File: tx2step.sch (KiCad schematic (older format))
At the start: 17 parts, among them IC1 ATMEGA328P-MM

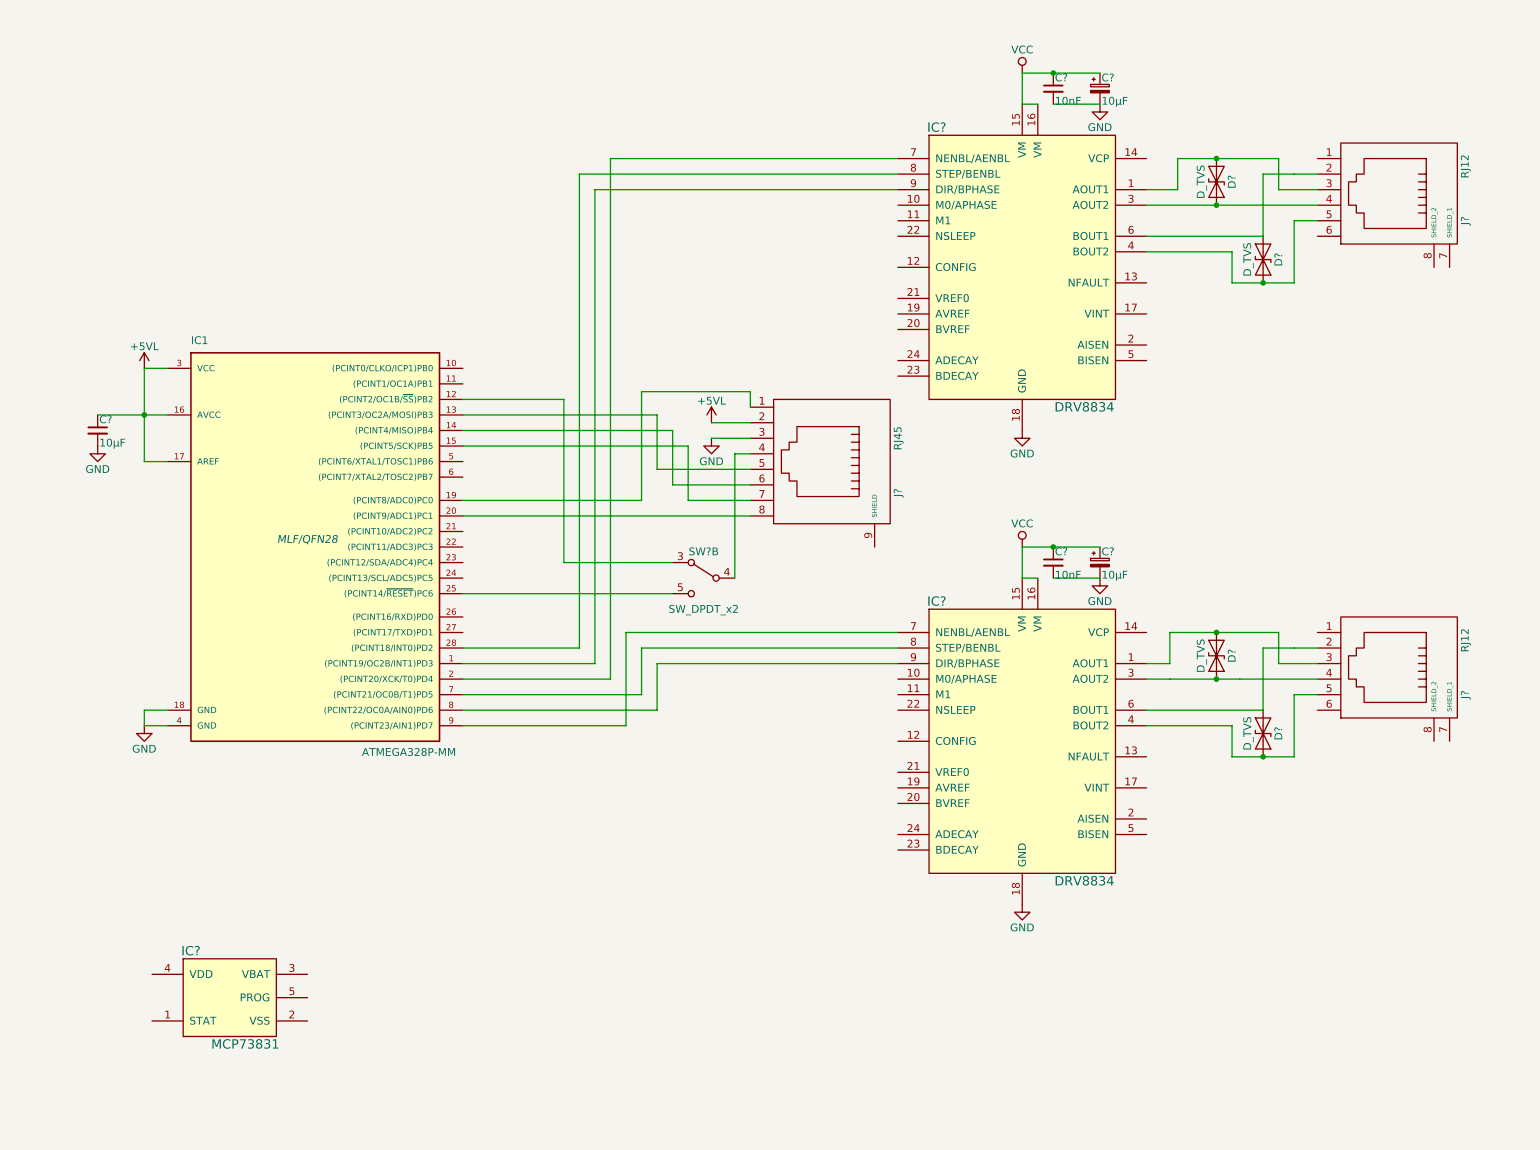
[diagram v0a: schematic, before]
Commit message: Add rate selector switches
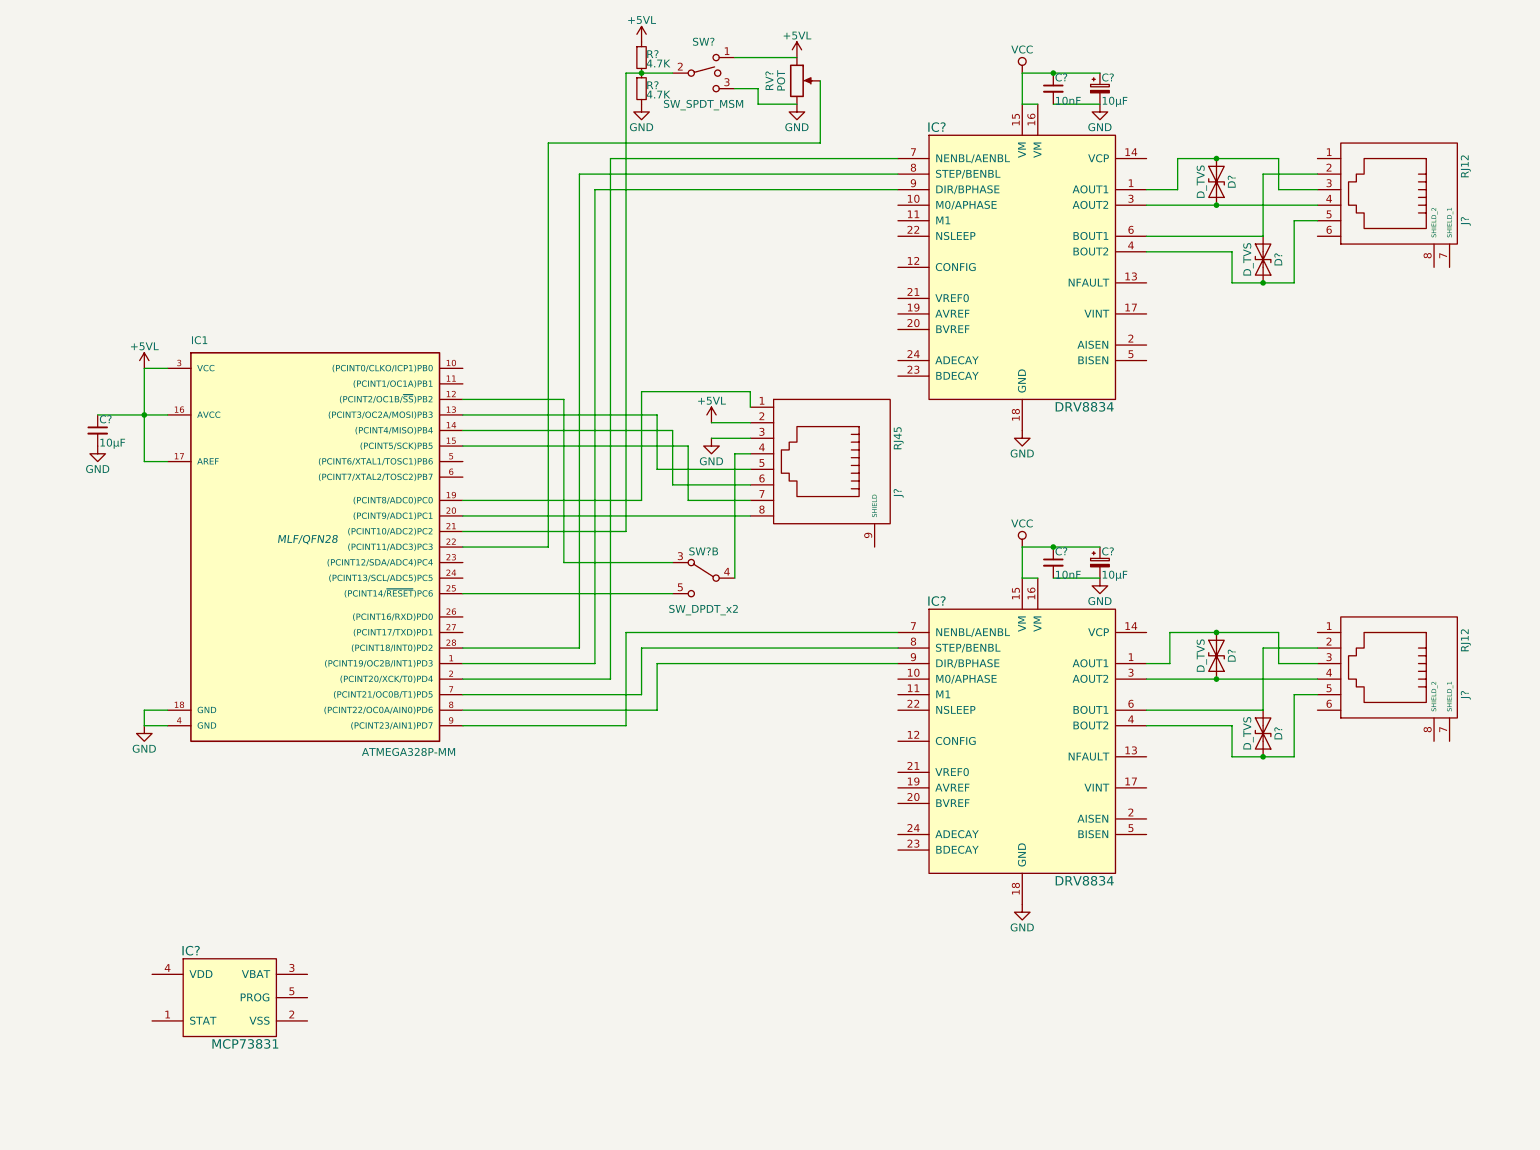
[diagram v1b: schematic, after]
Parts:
- added R? (x2): 4.7K, symbol R_Small
- added RV?: POT, symbol POT
- added SW?: SW_SPDT_MSM, symbol SW_SPDT_MSM
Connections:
- net +5VL: now also R?.1, RV?.1, SW?.1
- net GND: now also R?.2, RV?.3, SW?.3
- net at IC1.21 ((PCINT10/ADC2)PC2): now also R?.1, R?.2, SW?.2
- net at IC1.22 ((PCINT11/ADC3)PC3): now also RV?.2
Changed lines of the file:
@@
 	8150 1550 8150 1750
 Wire Wire Line
-	7950 1850 8400 1850
-Wire Wire Line
-	8400 1850 9050 1850
+	7950 1850 9050 1850
 Wire Wire Line
 	8800 1550 8800 1750
@@
 	8700 2050 8700 1650
 Wire Wire Line
-	8700 1650 8900 1650
-Wire Wire Line
-	8900 1650 8900 1650
-Wire Wire Line
-	8900 1650 9050 1650
+	8700 1650 9050 1650
 Wire Wire Line
 	9050 1950 8900 1950
 Wire Wire Line
-	8900 2350 8900 1950
-Wire Wire Line
-	8500 2350 8700 2350
-Wire Wire Line
-	8700 2350 8900 2350
+	8900 1950 8900 2350
+Wire Wire Line
+	8900 2350 8500 2350
 Wire Wire Line
 	8500 2350 8500 2150
@@
 	8100 4800 8100 4600
 Wire Wire Line
-	8100 4600 8400 4600
-Wire Wire Line
-	8400 4600 8800 4600
-Wire Wire Line
-	7950 4900 8100 4900
-Wire Wire Line
-	8100 4900 8100 4900
-Wire Wire Line
-	8100 4900 8400 4900
-Wire Wire Line
-	8400 4900 8550 4900
+	8100 4600 8800 4600
+Wire Wire Line
+	7950 4900 9050 4900
 Wire Wire Line
 	8800 4600 8800 4800
@@
 	8800 4800 9050 4800
 Connection ~ 8400 4600
-Wire Wire Line
-	8550 4900 8550 4900
-Wire Wire Line
-	8550 4900 9050 4900
 Connection ~ 8400 4900
 Wire Wire Line
@@
 	8500 5200 8500 5400
 Wire Wire Line
-	8500 5400 8700 5400
-Wire Wire Line
-	8700 5400 8900 5400
+	8500 5400 8900 5400
 Wire Wire Line
 	8700 5100 8700 4700
 Wire Wire Line
-	8700 4700 8900 4700
-Wire Wire Line
-	8900 4700 8900 4700
-Wire Wire Line
-	8900 4700 9050 4700
+	8700 4700 9050 4700
 Wire Wire Line
 	8900 5400 8900 5000
@@
 	4800 4800 6350 4800
 Wire Wire Line
-	1500 2900 1500 3200
-Wire Wire Line
-	1500 3200 1500 3500
-Wire Wire Line
-	1200 3200 1500 3200
-Wire Wire Line
-	1500 3200 1650 3200
+	1500 2900 1500 3500
+Wire Wire Line
+	1200 3200 1650 3200
 Connection ~ 1500 3200
 Wire Wire Line
@@
 	7150 4250 7250 4250
 Wire Wire Line
-	7150 1000 7350 1000
-Wire Wire Line
-	7350 1000 7650 1000
+	7150 1000 7650 1000
 Wire Wire Line
 	7150 1000 7150 1200
@@
 	7350 1200 7650 1200
 Wire Wire Line
-	7150 4050 7350 4050
-Wire Wire Line
-	7350 4050 7650 4050
+	7150 4050 7650 4050
 Wire Wire Line
 	7650 4250 7350 4250
@@
 $EndComp
 Wire Wire Line
-	8150 1550 8400 1550
-Wire Wire Line
-	8400 1550 8800 1550
+	8150 1550 8800 1550
 Connection ~ 8400 1550
 $Comp
@@
 	1    0    0    -1
 $EndComp
+$Comp
+L SW_SPDT_MSM SW?
+U 1 1 58B86814
+P 5100 1000
+F 0 "SW?" H 5100 1200 50  0000 C CNN
+F 1 "SW_SPDT_MSM" H 5100 800 50  0000 C CNN
+F 2 "" H 5100 1000 50  0001 C CNN
+F 3 "" H 5100 1000 50  0001 C CNN
+	1    5100 1000
+	1    0    0    -1
+$EndComp
+$Comp
+L POT RV?
+U 1 1 58B868AD
+P 5700 1050
+F 0 "RV?" V 5525 1050 50  0000 C CNN
+F 1 "POT" V 5600 1050 50  0000 C CNN
+F 2 "" H 5700 1050 50  0000 C CNN
+F 3 "" H 5700 1050 50  0000 C CNN
+	1    5700 1050
+	1    0    0    -1
+$EndComp
+Wire Wire Line
+	5300 900  5700 900
+Wire Wire Line
+	5300 1100 5450 1100
+Wire Wire Line
+	5450 1100 5450 1200
+Wire Wire Line
+	5450 1200 5700 1200
+$Comp
+L +5VL #PWR?
+U 1 1 58B874D3
+P 5700 900
+F 0 "#PWR?" H 5700 750 50  0001 C CNN
+F 1 "+5VL" H 5700 1040 50  0000 C CNN
+F 2 "" H 5700 900 50  0000 C CNN
+F 3 "" H 5700 900 50  0000 C CNN
+	1    5700 900
+	1    0    0    -1
+$EndComp
+$Comp
+L GND #PWR?
+U 1 1 58B87520
+P 5700 1200
+F 0 "#PWR?" H 5700 950 50  0001 C CNN
+F 1 "GND" H 5700 1050 50  0000 C CNN
+F 2 "" H 5700 1200 50  0000 C CNN
+F 3 "" H 5700 1200 50  0000 C CNN
+	1    5700 1200
+	1    0    0    -1
+$EndComp
+$Comp
+L R_Small R?
+U 1 1 58B876D6
+P 4700 900
+F 0 "R?" H 4730 920 50  0000 L CNN
+F 1 "4.7K" H 4730 860 50  0000 L CNN
+F 2 "" H 4700 900 50  0000 C CNN
+F 3 "" H 4700 900 50  0000 C CNN
+	1    4700 900
+	1    0    0    -1
+$EndComp
+$Comp
+L R_Small R?
+U 1 1 58B87737
+P 4700 1100
+F 0 "R?" H 4730 1120 50  0000 L CNN
+F 1 "4.7K" H 4730 1060 50  0000 L CNN
+F 2 "" H 4700 1100 50  0000 C CNN
+F 3 "" H 4700 1100 50  0000 C CNN
+	1    4700 1100
+	1    0    0    -1
+$EndComp
+Wire Wire Line
+	4600 1000 4900 1000
+Wire Wire Line
+	4600 3950 3550 3950
+Connection ~ 4700 1000
+Wire Wire Line
+	4100 4050 3550 4050
+Wire Wire Line
+	4100 1450 5850 1450
+Wire Wire Line
+	5850 1450 5850 1050
+$Comp
+L GND #PWR?
+U 1 1 58B895AD
+P 4700 1200
+F 0 "#PWR?" H 4700 950 50  0001 C CNN
+F 1 "GND" H 4700 1050 50  0000 C CNN
+F 2 "" H 4700 1200 50  0000 C CNN
+F 3 "" H 4700 1200 50  0000 C CNN
+	1    4700 1200
+	1    0    0    -1
+$EndComp
+$Comp
+L +5VL #PWR?
+U 1 1 58B89600
+P 4700 800
+F 0 "#PWR?" H 4700 650 50  0001 C CNN
+F 1 "+5VL" H 4700 940 50  0000 C CNN
+F 2 "" H 4700 800 50  0000 C CNN
+F 3 "" H 4700 800 50  0000 C CNN
+	1    4700 800
+	1    0    0    -1
+$EndComp
+Wire Wire Line
+	4100 1450 4100 4050
+Wire Wire Line
+	4600 1000 4600 3950
 $EndSCHEMATC

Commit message: Add clock crystal
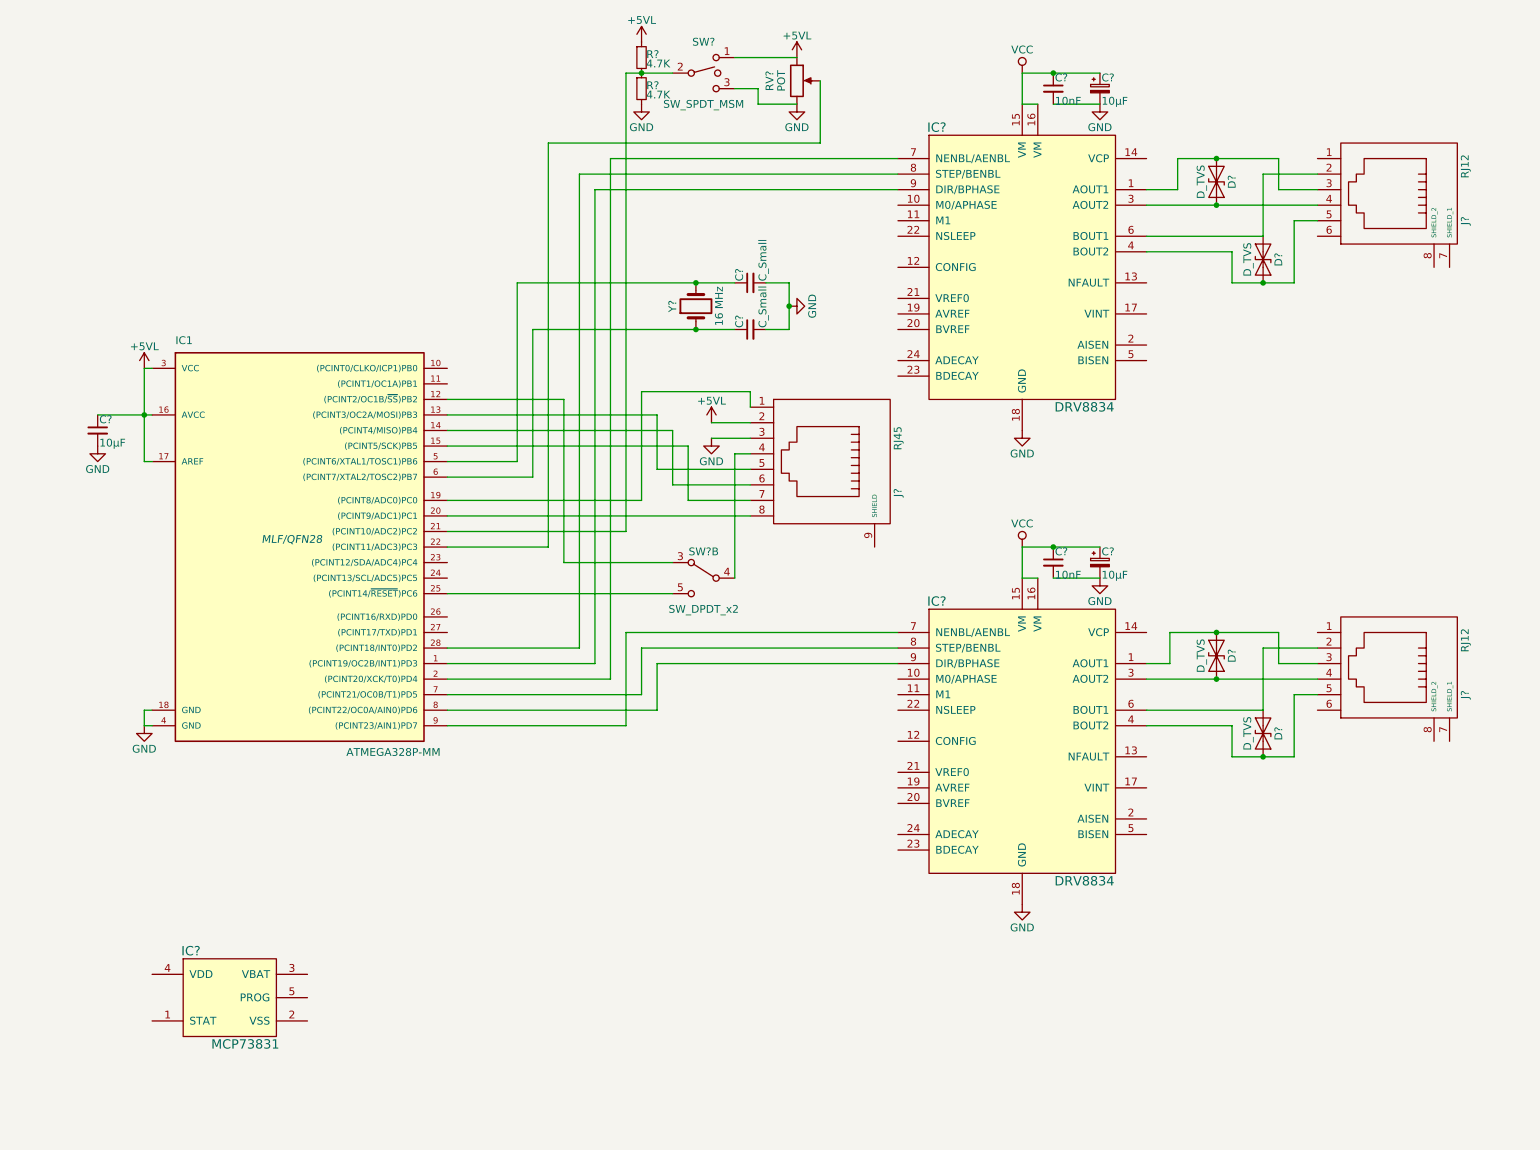
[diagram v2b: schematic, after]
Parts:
- added C? (x2): C_Small, symbol C_Small
- added Y?: 16 MHz, symbol Crystal
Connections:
- net GND: now also C?.2, C?.2
- net at IC1.5 ((PCINT6/XTAL1/TOSC1)PB6): now also C?.1, Y?.2
- net at IC1.6 ((PCINT7/XTAL2/TOSC2)PB7): now also C?.1, Y?.1
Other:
- moved on the sheet: IC1

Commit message: Fully wire up DRV8834 chips
The selection of external supporting components is based in part on
the example application circuit in the DRV8834 datasheet, and in part
on the design of the Pololu DRV8834 breakout board.

The voltage divider and current sense resistor values listed in the
schematic should program a current limit of 117mA per phase, which is
in line with the current limit selected by the potentiometers in the
prototype. The voltage divider resistors will probably be installed in
a DIP socket to allow reconfiguring the current limit by replacing
resistors (slightly less convenient than a potentiometer, but also
slightly more permanent.)
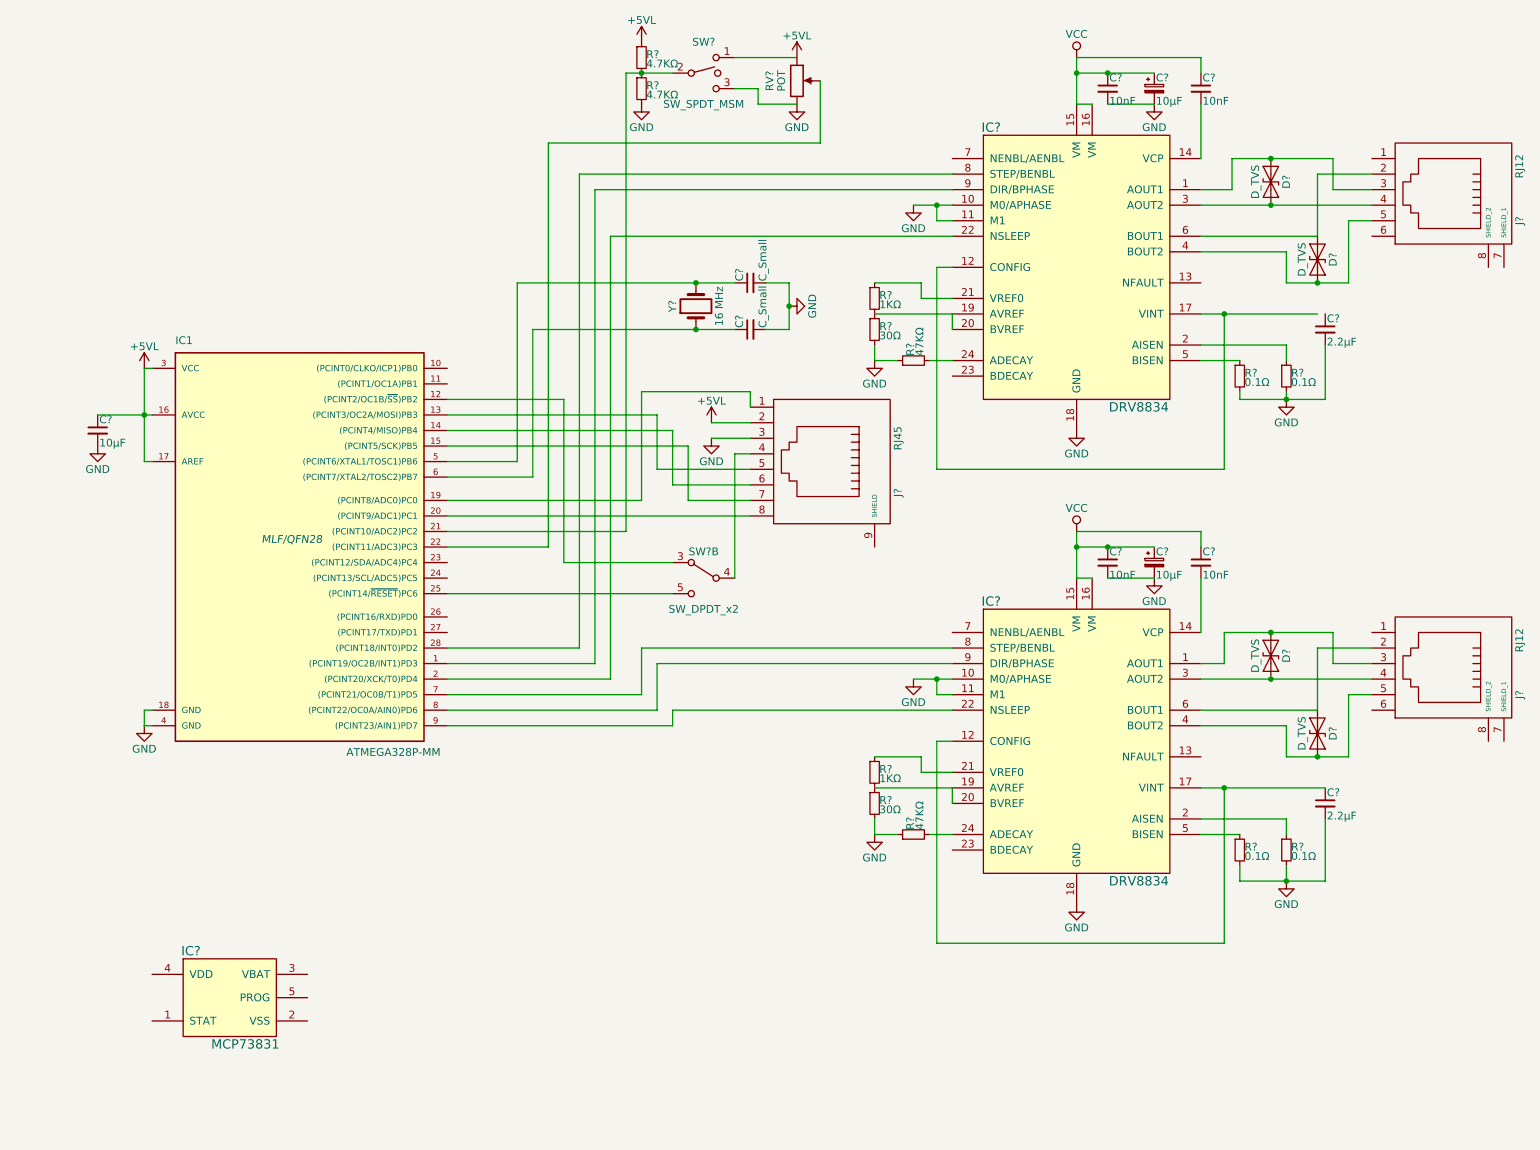
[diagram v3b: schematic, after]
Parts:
- added C? (x2): 10nF, symbol C_Small
- added C? (x2): 2.2µF, symbol C_Small
- added R? (x2): 47KΩ, symbol R_Small
- added R? (x4): 0.1Ω, symbol R_Small
- added R? (x2): 1KΩ, symbol R_Small
- added R? (x2): 30Ω, symbol R_Small
- R? (x2): value 4.7K -> 4.7KΩ
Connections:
- net GND: now also IC?.10 (M0/APHASE), IC?.10 (M0/APHASE), IC?.11 (M1), IC?.11 (M1), C?.2, C?.2, R?.1, R?.1, R?.2, R?.2, R?.2, R?.2, R?.2, R?.2
- net VCC: now also C?.1, C?.1
- net at IC1.2 ((PCINT20/XCK/T0)PD4): now also IC?.22 (NSLEEP); no longer IC?.7 (NENBL/AENBL)
- net at IC1.9 ((PCINT23/AIN1)PD7): now also IC?.22 (NSLEEP); no longer IC?.7 (NENBL/AENBL)
- net at IC?.12 (CONFIG): now also IC?.17 (VINT)
- net at IC?.14 (VCP): now also C?.2 (x2)
- net at IC?.19 (AVREF): now also IC?.20 (BVREF), R?.1, R?.2 (x2)
- net at IC?.2 (AISEN): now also R?.1 (x2)
- net at IC?.21 (VREF0): now also R?.1 (x2)
- net at IC?.24 (ADECAY): now also R?.2 (x2)
- net at IC?.5 (BISEN): now also R?.1 (x2)
- net at IC?.12 (CONFIG): now also IC?.17 (VINT), C?.1
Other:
- moved on the sheet: C?, D?, IC?, J?
